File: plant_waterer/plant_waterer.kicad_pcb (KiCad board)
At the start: 2 copper layers, 59.1 x 41.3 mm, 30 parts, among them J1 Conn_01x02, J2 Conn_01x02, J3 PJ-002AH, J4 Conn_01x03, U1 TB6612FNG,C,8,EL, U2 OLED_DISP, U3 XIAO_RP2040, U4 ESD7002, U5 AP2204R-5.0TRG1

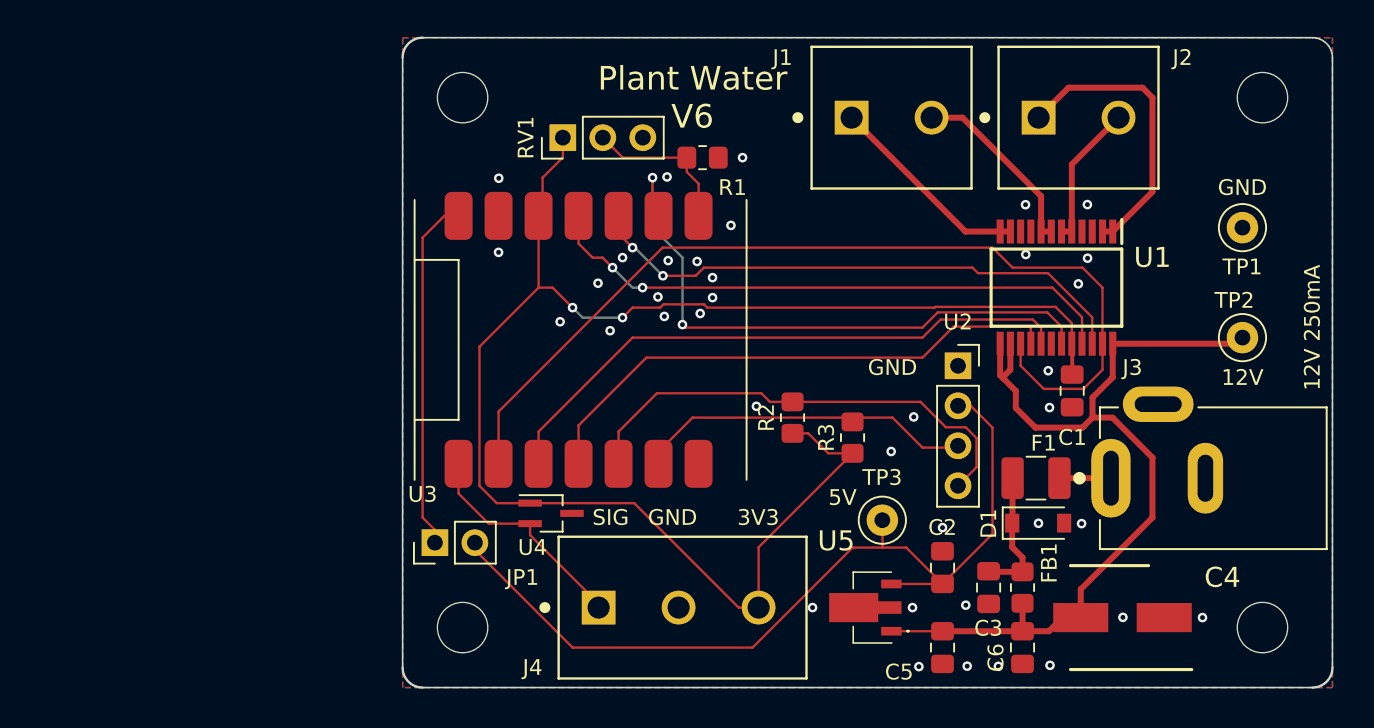
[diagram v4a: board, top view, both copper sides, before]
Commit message: Switched pot to ADC pin
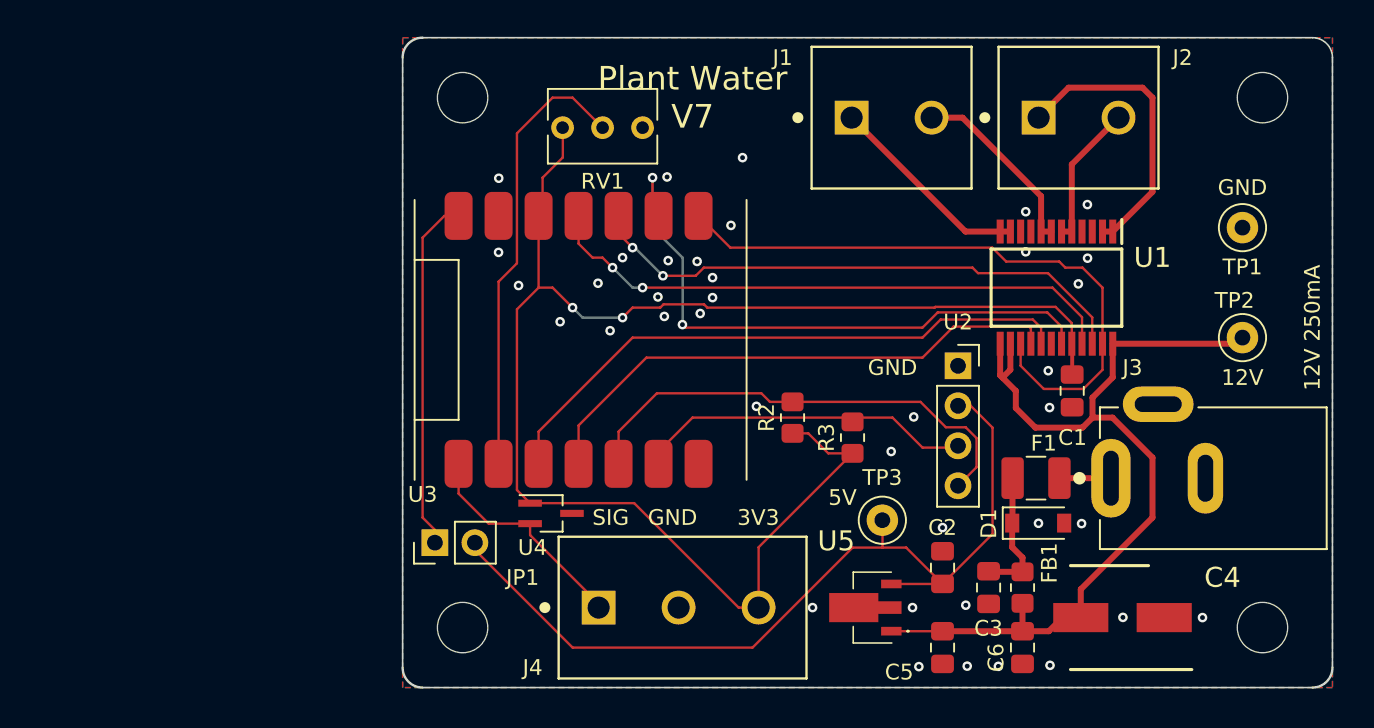
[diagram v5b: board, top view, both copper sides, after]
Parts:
- removed R1: 10K, Resistor_SMD:R_0805_2012Metric_Pad1.20x1.40mm_HandSolder
- RV1: value 100K -> R_Potentiometer; footprint Connector_PinHeader_2.54mm:PinHeader_1x03_P2.54mm_Vertical -> Potentiometer_THT:Potentiometer_Bourns_3266Y_Vertical
- moved RV1 0.64 mm to (71.1, 40.6), turned to 180 degrees
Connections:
- RV1 pad 2: Net-(R1-Pad1) -> Net-(U3-Pad1)
- RV1 pad 3: (no net) -> GND
- U3 pad 1: /PWMA -> Net-(U3-Pad1)
- U3 pad 7: Net-(R1-Pad1) -> /PWMA
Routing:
- net Net-(U3-Pad1): track 0.00 -> 28.6 mm
- net /PWMA: track 60.0 -> 40.5 mm
- net Net-(R1-Pad1): track 9.87 -> 0.00 mm
- net +3.3V: track 100.0 -> 96.8 mm
- net GND: vias 38 -> 39
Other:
- board text added: "Plant Water V7"
- board text removed: "Plant Water V6"

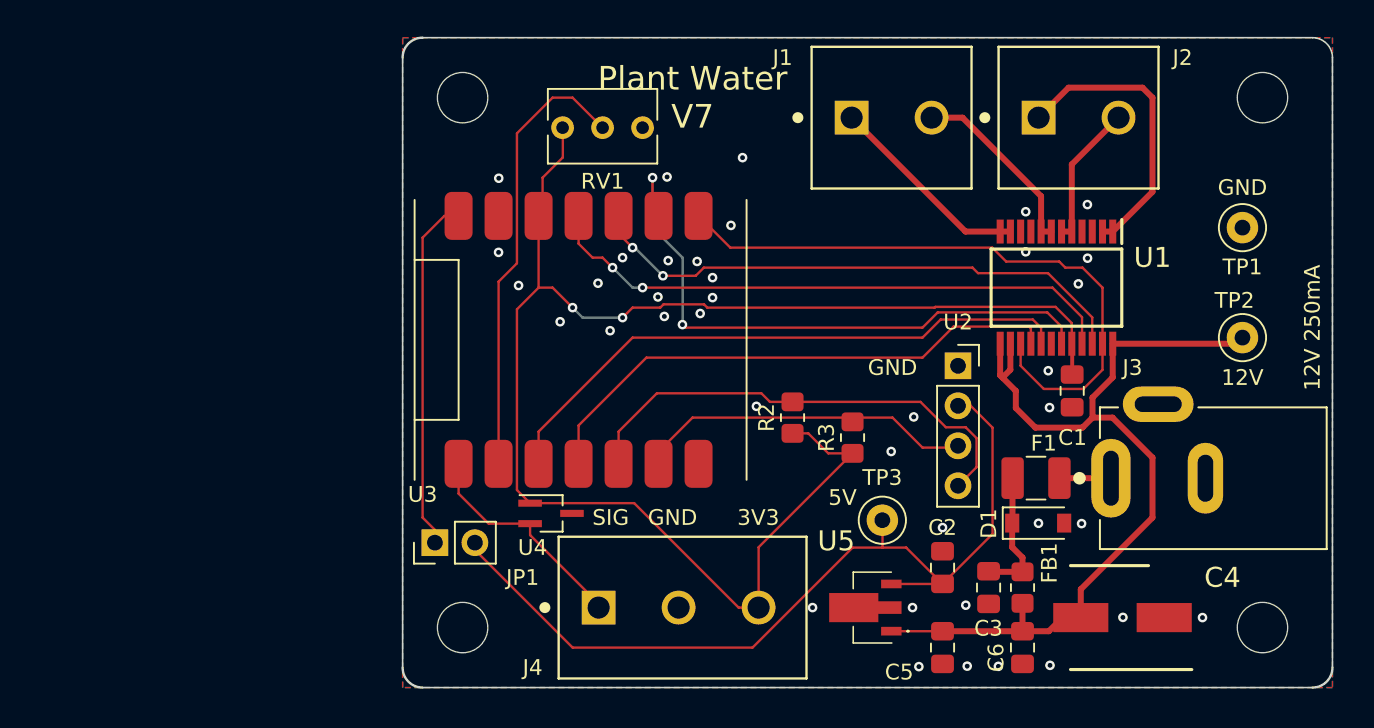
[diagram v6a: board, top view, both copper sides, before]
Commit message: Swapped in RPi Pico W
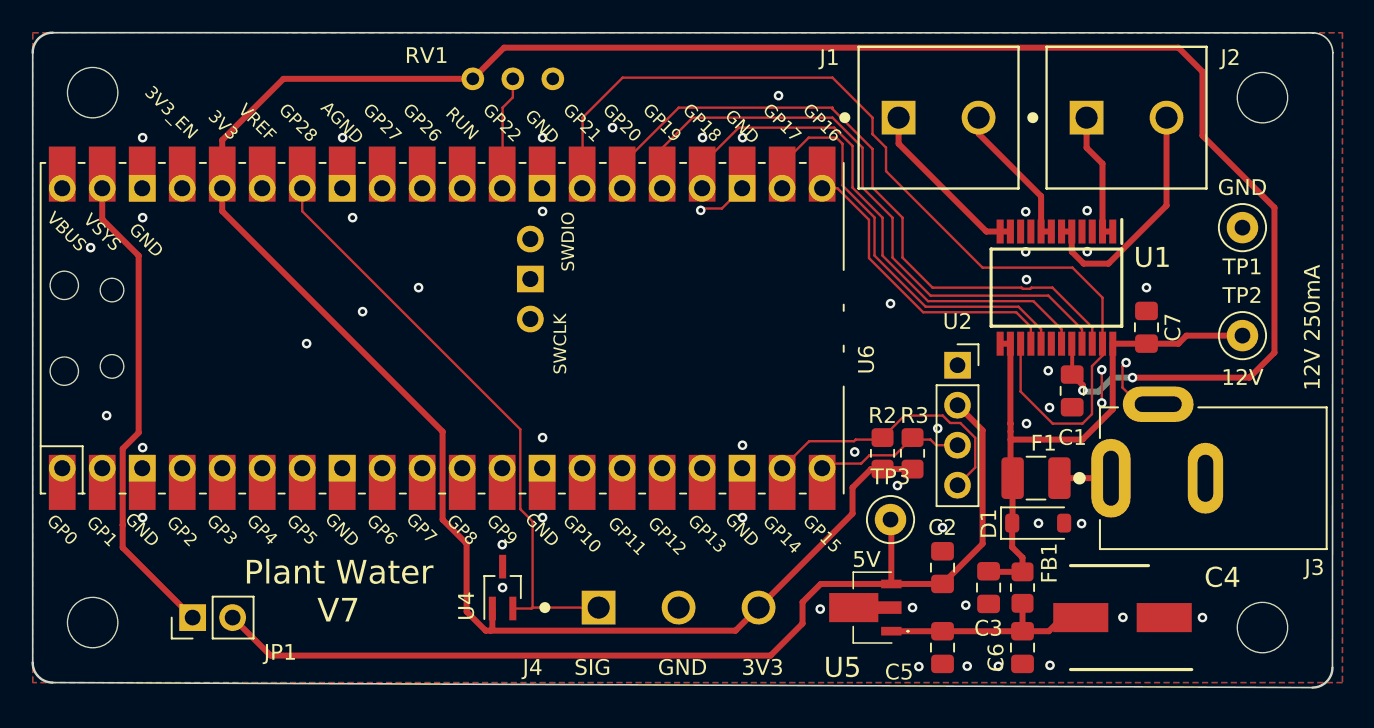
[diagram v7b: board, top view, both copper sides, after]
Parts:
- removed U3: XIAO_RP2040, Library:XIAO RP2040
- added C7: 10uF, Capacitor_SMD:C_0805_2012Metric_Pad1.18x1.45mm_HandSolder, F.Cu at (108.2, 53.3)
- added U6: PicoW, RPi_Pico:RPi_PicoW_SMD_TH, F.Cu at (63.5, 53.4)
- F1: value Polyfuse_Small -> 160ma
- moved REF** 23.5 mm to (41.3, 72.1)
- moved REF** 23.5 mm to (41.3, 38.4)
- moved JP1 16.1 mm to (47.6, 71.8)
- moved RV1 6.49 mm to (65.4, 37.5)
- moved R2 6.15 mm to (91.4, 61.3)
- moved U4 5.63 mm to (67.3, 69.8), turned to 90 degrees
- moved R3 3.94 mm to (93.3, 61.3)
- moved J2 3.05 mm to (109.7, 40.0)
- moved J1 2.98 mm to (97.8, 40.0)
- moved TP3 0.52 mm to (91.9, 65.5)
- moved TP2 0.13 mm to (114.3, 53.8), turned to 0 degrees
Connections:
- C3 pad 2: /VIN -> +12P
- D1 pad 1: /VIN -> +12P
- F1 pad 2: /VIN -> +12P
- FB1 pad 1: /VIN -> +12P
- JP1 pad 1: Net-(JP1-Pad1) -> /5V_JUMP
- TP2 pad 1: +12V -> +12P
- U1 pad 13: +12V -> +12P
- U1 pad 14: +12V -> +12P
- U1 pad 24: +12V -> +12P
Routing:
- net +3.3V: track 96.8 -> 173.4 mm
- net +12V: track 57.2 -> 14.2 mm
- net +12P: track 0.00 -> 37.0 mm
- net /5V_JUMP: track 0.00 -> 30.5 mm
- net Net-(J4-Pin_1): track 14.4 -> 38.2 mm
- net Net-(JP1-Pad1): track 22.6 -> 0.00 mm
- net /PWMA: track 40.5 -> 62.2 mm
- net Net-(U6-GPIO22): track 28.6 -> 7.23 mm
- net /BIN2: track 34.8 -> 19.4 mm
- net Net-(U2-SDA): track 30.5 -> 17.7 mm
- net Net-(U2-SCK): track 21.4 -> 9.50 mm
- net +5V: track 54.8 -> 65.9 mm
- net /BIN1: track 38.1 -> 27.6 mm
- net /AO1: track 18.5 -> 8.30 mm
- net GND: track 0.00 -> 9.71 mm, vias 39 -> 52
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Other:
- board size 59.1 x 41.3 mm -> 82.6 x 41.6 mm

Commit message: Switched to different motor driver ZXBM5210-SP-13
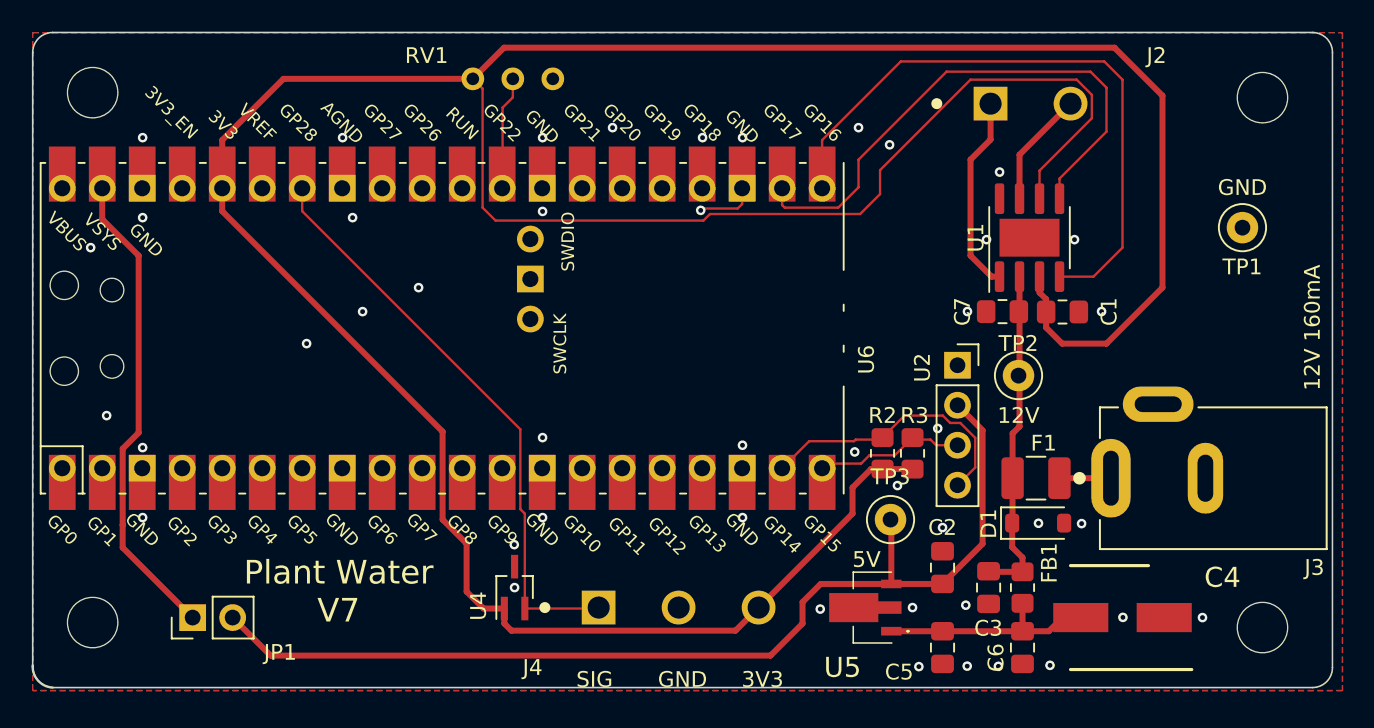
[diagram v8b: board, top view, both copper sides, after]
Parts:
- removed J1: Conn_01x02, Library:CONN 1x2 5mm
- U1: value TB6612FNG,C,8,EL -> ZXBM5210-SP-13; footprint Library:SOP65P760X160-24N -> Package_SO:SOIC-8-1EP_3.9x4.9mm_P1.27mm_EP2.41x3.81mm
- moved TP2 14.4 mm to (100.1, 56.4)
- moved C7 9.20 mm to (99.1, 52.3), turned to 0 degrees
- moved J2 6.16 mm to (103.6, 39.1)
- moved C1 5.05 mm to (102.9, 52.3), turned to 180 degrees
- moved U1 3.60 mm to (100.8, 47.6), turned to 90 degrees
- moved U4 0.76 mm to (68.1, 69.8)
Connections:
- U1 pad 2: /AO1 -> +12P
- U1 pad 3: GND -> +3.3V
- U1 pad 4: GND -> /AIN1
- U1 pad 5: /AO2 -> /AIN2
- U1 pad 6: /AO2 -> +3.3V
- U1 pad 7: /BO2 -> /AO2
- U1 pad 8: /BO2 -> GND
- U6 pad 21: /BIN2 -> /AIN1
- U6 pad 22: /BIN1 -> /AIN2
- U6 pad 24: /STBY -> unconnected-(U6-GPIO18-Pad24)
- U6 pad 25: /AIN1 -> unconnected-(U6-GPIO19-Pad25)
- U6 pad 26: /AIN2 -> unconnected-(U6-GPIO20-Pad26)
- U6 pad 27: /PWMA -> unconnected-(U6-GPIO21-Pad27)
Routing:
- net /PWMA: track 62.2 -> 0.00 mm
- net +3.3V: track 173.4 -> 219.0 mm, vias 2 -> 0
- net /STBY: track 34.5 -> 0.00 mm
- net /BIN1: track 27.6 -> 0.00 mm
- net /BIN2: track 19.4 -> 0.00 mm
- net +12P: track 37.0 -> 20.8 mm
- net /B01: track 11.1 -> 0.00 mm
- net /BO2: track 9.53 -> 0.00 mm
- net /AO2: track 15.4 -> 7.38 mm
- net /AIN2: track 42.7 -> 35.1 mm
- net GND: track 9.71 -> 5.01 mm, vias 52 -> 45
- net /AO1: track 8.30 -> 12.6 mm
- net Net-(J4-Pin_1): track 38.2 -> 37.3 mm
- net /AIN1: track 39.5 -> 40.1 mm
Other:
- board size 82.6 x 41.6 mm -> 82.5 x 41.6 mm
- board text added: "12V 160mA"
- board text removed: "12V 250mA"
